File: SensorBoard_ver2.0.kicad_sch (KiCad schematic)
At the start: 64 parts, among them J1 CANConn, J10 Limit3-B, J11 USB_C, J12 Limit2-A, J13 Limit2-B, J14 Limit4-A, J15 Limit4-B, J16 Abso, J17 Abso, J18 STLink, J19 Abso, J2 CANConn, J20 Abso, J21 Abso, J22 Abso, J3 Enc1, J4 Enc2, J5 Enc3, J6 Enc4, J7 Limit1-A, J8 Limit1-B, J9 Limit3-A, SW1 CAN_Terminal, SW2 IDSetSW, SW3 Enc⇔Lim Change, SW4 ResetSW, SW5 RS485_Terminal, SW6 AbsoSW, U1 L7805, U2 ATA6561, U3 3.3V Regulator, U4 STM32F303K8Tx, U5 MAX3485, Y1 Crystal

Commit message: Add files via upload
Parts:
- removed J10: Limit3-B, Connector_JST:JST_XA_B02B-XASK-1_1x02_P2.50mm_Vertical, symbol Connector:Conn_01x02_Socket
- removed J12: Limit2-A, Connector_JST:JST_XA_B02B-XASK-1_1x02_P2.50mm_Vertical, symbol Connector:Conn_01x02_Socket
- removed J13: Limit2-B, Connector_JST:JST_XA_B02B-XASK-1_1x02_P2.50mm_Vertical, symbol Connector:Conn_01x02_Socket
- removed J14: Limit4-A, Connector_JST:JST_XA_B02B-XASK-1_1x02_P2.50mm_Vertical, symbol Connector:Conn_01x02_Socket
- removed J15: Limit4-B, Connector_JST:JST_XA_B02B-XASK-1_1x02_P2.50mm_Vertical, symbol Connector:Conn_01x02_Socket
- removed J7: Limit1-A, Connector_JST:JST_XA_B02B-XASK-1_1x02_P2.50mm_Vertical, symbol Connector:Conn_01x02_Socket
- removed J8: Limit1-B, Connector_JST:JST_XA_B02B-XASK-1_1x02_P2.50mm_Vertical, symbol Connector:Conn_01x02_Socket
- removed J9: Limit3-A, Connector_JST:JST_XA_B02B-XASK-1_1x02_P2.50mm_Vertical, symbol Connector:Conn_01x02_Socket
- added J?: LimitConn, Connector_JST:JST_XA_S05B-XASK-1_1x05_P2.50mm_Horizontal, symbol Connector:Conn_01x05_Socket
- J20: value Abso -> VCP
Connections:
- net IDSetSW is gone; now on net IDSet: U4.28 (PB5)
- net EncA_4: now also U4.14 (PB0)
- net EncB_4: now also U4.15 (PB1)
- net GND: now also J?.5 (Pin_5)
- net LED1: now also U4.29 (PB6); no longer U4.14 (PB0)
- net LED2: now also U4.30 (PB7); no longer U4.15 (PB1)
- net UARTTX: no longer U4.29 (PB6), U4.30 (PB7)

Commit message: 回路図の更新・PCBを作成
そんなもん
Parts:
- removed SW3: Enc⇔Lim Change, Connector_PinHeader_2.54mm:PinHeader_1x03_P2.54mm_Vertical, symbol Switch:SW_Nidec_CAS-120A1
- added J11: Limit4, Connector_JST:JST_XA_S02B-XASK-1_1x02_P2.50mm_Horizontal, symbol Connector:Conn_01x02_Socket
- added J12: Limit3, Connector_JST:JST_XA_S02B-XASK-1_1x02_P2.50mm_Horizontal, symbol Connector:Conn_01x02_Socket
- added J20: Enc5, Connector_JST:JST_XA_S04B-XASK-1_1x04_P2.50mm_Horizontal, symbol Connector:Conn_01x04_Socket
- added J8: Limit1, Connector_JST:JST_XA_S02B-XASK-1_1x02_P2.50mm_Horizontal, symbol Connector:Conn_01x02_Socket
- added J9: Limit2, Connector_JST:JST_XA_S02B-XASK-1_1x02_P2.50mm_Horizontal, symbol Connector:Conn_01x02_Socket
- added JP2: FB-Short, Jumper:SolderJumper-2_P1.3mm_Open_TrianglePad1.0x1.5mm, symbol Jumper:SolderJumper_2_Open
- J17: renamed from J20; footprint Connector_JST:JST_XA_S04B-XASK-1_1x04_P2.50mm_Horizontal -> Connector_JST:JST_XA_B04B-XASK-1_1x04_P2.50mm_Vertical
- JP1: footprint Jumper:SolderJumper-2_P1.3mm_Open_RoundedPad1.0x1.5mm -> Jumper:SolderJumper-2_P1.3mm_Open_TrianglePad1.0x1.5mm
- gave numbers to parts that had none: 1
- renumbered J11 to J10, J16 to J13, J17 to J14, J18 to J15, J19 to J16, J21 to J18, J22 to J19
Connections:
- net +3.3V: now also JP2.1 (A)
- net +3.3VA: now also JP2.2 (B)
- net +5V: now also J20.1 (Pin_1)
- net GND: now also J11.2 (Pin_2), J12.2 (Pin_2), J20.4 (Pin_4), J8.2 (Pin_2), J9.2 (Pin_2)
- net Limit1: now reaches J7.1 (Pin_1)
- net Limit1: now also J8.1 (Pin_1)
- net Limit2: now reaches J7.2 (Pin_2)
- net Limit2: now also J9.1 (Pin_1)
- net Limit3: now reaches J7.3 (Pin_3)
- net Limit3: now also J12.1 (Pin_1)
- net Limit4: now reaches J7.4 (Pin_4)
- net Limit4: now also J11.1 (Pin_1)
- net LED1 renamed EncA_5
- net EncA_5: now also J20.2 (Pin_2)
- net LED2 renamed EncB_5
- net EncB_5: now also J20.3 (Pin_3)
- net LimitMode: no longer names the net of U4.9 (PA3)
- no-connect marks 5 -> 4
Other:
- note removed: "Enc⇔Limit Change"
- moved on the sheet: J17, J7

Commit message: 基板作成
締まらない、なんか違う
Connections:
- net +3.3V: now also U3.4 (OUT)
- net AbsoSW: now also U4.6 (PA0); no longer U4.27 (PB4)
- net EncA_1: now also U4.27 (PB4); no longer U4.6 (PA0)
- net EncB_1: now also U4.28 (PB5); no longer U4.7 (PA1)
- net IDSet: now also U4.7 (PA1); no longer U4.28 (PB5)
- net LED: now reaches U4.9 (PA3)
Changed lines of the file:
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@@
 	)
 	(junction
+		(at 91.44 82.55)
+		(diameter 0)
+		(color 0 0 0 0)
+	)
+	(junction
 		(at 222.25 151.13)
 		(diameter 0)
@@
 	)
 	(junction
-		(at 91.44 83.82)
+		(at 109.22 81.28)
 		(diameter 0)
 		(color 0 0 0 0)
@@
 	(wire
 		(pts
-			(xy 125.73 66.04) (xy 133.35 66.04)
-		)
-		(stroke
-			(width 0)
-			(type default)
-		)
-	)
-	(wire
-		(pts
 			(xy 223.52 125.73) (xy 224.79 125.73)
 		)
@@
 	(wire
 		(pts
+			(xy 91.44 82.55) (xy 91.44 83.82)
+		)
+		(stroke
+			(width 0)
+			(type default)
+		)
+	)
+	(wire
+		(pts
 			(xy 26.67 50.8) (xy 25.4 50.8)
 		)
@@
 	(wire
 		(pts
-			(xy 91.44 82.55) (xy 91.44 83.82)
+			(xy 91.44 81.28) (xy 91.44 82.55)
 		)
 		(stroke
@@
 	(wire
 		(pts
-			(xy 163.83 48.26) (xy 172.72 48.26)
-		)
-		(stroke
-			(width 0)
-			(type default)
-		)
-	)
-	(wire
-		(pts
 			(xy 125.73 60.96) (xy 133.35 60.96)
 		)
@@
 	(wire
 		(pts
+			(xy 109.22 81.28) (xy 109.22 83.82)
+		)
+		(stroke
+			(width 0)
+			(type default)
+		)
+	)
+	(wire
+		(pts
 			(xy 58.42 87.63) (xy 58.42 88.9)
 		)
@@
 	(wire
 		(pts
+			(xy 125.73 66.04) (xy 133.35 66.04)
+		)
+		(stroke
+			(width 0)
+			(type default)
+		)
+	)
+	(wire
+		(pts
 			(xy 46.99 173.99) (xy 45.72 173.99)
 		)
@@
 	(wire
 		(pts
+			(xy 107.95 81.28) (xy 109.22 81.28)
+		)
+		(stroke
+			(width 0)
+			(type default)
+		)
+	)
+	(wire
+		(pts
+			(xy 163.83 40.64) (xy 172.72 40.64)
+		)
+		(stroke
+			(width 0)
+			(type default)
+		)
+	)
+	(wire
+		(pts
 			(xy 207.01 64.77) (xy 207.01 66.04)
 		)
@@
 	(wire
 		(pts
-			(xy 163.83 43.18) (xy 172.72 43.18)
+			(xy 205.74 88.9) (xy 205.74 91.44)
 		)
 		(stroke
@@
 	(wire
 		(pts
-			(xy 205.74 88.9) (xy 205.74 91.44)
+			(xy 243.84 125.73) (xy 245.11 125.73)
 		)
 		(stroke
@@
 	(wire
 		(pts
-			(xy 243.84 125.73) (xy 245.11 125.73)
+			(xy 163.83 48.26) (xy 172.72 48.26)
 		)
 		(stroke
@@
 	(wire
 		(pts
-			(xy 91.44 83.82) (xy 92.71 83.82)
-		)
-		(stroke
-			(width 0)
-			(type default)
-		)
-	)
-	(wire
-		(pts
 			(xy 215.9 55.88) (xy 217.17 55.88)
 		)
@@
 	(wire
 		(pts
-			(xy 40.64 83.82) (xy 39.37 83.82)
+			(xy 91.44 82.55) (xy 92.71 82.55)
 		)
 		(stroke
@@
 	(wire
 		(pts
-			(xy 261.62 151.13) (xy 267.97 151.13)
+			(xy 40.64 83.82) (xy 39.37 83.82)
 		)
 		(stroke
@@
 	(wire
 		(pts
-			(xy 39.37 168.91) (xy 46.99 168.91)
+			(xy 261.62 151.13) (xy 267.97 151.13)
 		)
 		(stroke
@@
 	(wire
 		(pts
-			(xy 267.97 156.21) (xy 267.97 153.67)
+			(xy 39.37 168.91) (xy 46.99 168.91)
 		)
 		(stroke
@@
 	(wire
 		(pts
-			(xy 205.74 156.21) (xy 204.47 156.21)
+			(xy 267.97 156.21) (xy 267.97 153.67)
 		)
 		(stroke
@@
 	(wire
 		(pts
-			(xy 109.22 82.55) (xy 109.22 83.82)
+			(xy 205.74 156.21) (xy 204.47 156.21)
 		)
 		(stroke
@@
 	(wire
 		(pts
+			(xy 163.83 43.18) (xy 172.72 43.18)
+		)
+		(stroke
+			(width 0)
+			(type default)
+		)
+	)
+	(wire
+		(pts
 			(xy 240.03 153.67) (xy 240.03 156.21)
 		)
@@
 	(wire
 		(pts
+			(xy 125.73 68.58) (xy 133.35 68.58)
+		)
+		(stroke
+			(width 0)
+			(type default)
+		)
+	)
+	(wire
+		(pts
 			(xy 125.73 40.64) (xy 133.35 40.64)
 		)
@@
 	(wire
 		(pts
-			(xy 163.83 40.64) (xy 172.72 40.64)
-		)
-		(stroke
-			(width 0)
-			(type default)
-		)
-	)
-	(wire
-		(pts
 			(xy 67.31 173.99) (xy 66.04 173.99)
 		)
@@
 	(wire
 		(pts
-			(xy 125.73 68.58) (xy 133.35 68.58)
-		)
-		(stroke
-			(width 0)
-			(type default)
-		)
-	)
-	(wire
-		(pts
 			(xy 59.69 168.91) (xy 67.31 168.91)
 		)
@@
 		)
 	)
+	(label "IDSet"
+		(at 172.72 43.18 180)
+		(effects
+			(font
+				(size 1.27 1.27)
+			)
+			(justify right bottom)
+		)
+	)
 	(label "EncB_4"
 		(at 125.73 60.96 0)
@@
 		)
 	)
-	(label "EncA_1"
-		(at 172.72 40.64 180)
-		(effects
-			(font
-				(size 1.27 1.27)
-			)
-			(justify right bottom)
-		)
-	)
 	(label "CANL"
 		(at 33.02 55.88 180)
@@
 		)
 	)
+	(label "AbsoSW"
+		(at 172.72 40.64 180)
+		(effects
+			(font
+				(size 1.27 1.27)
+			)
+			(justify right bottom)
+		)
+	)
 	(label "CANL"
 		(at 33.02 34.29 180)
@@
 		)
 	)
+	(label "EncB_1"
+		(at 125.73 68.58 0)
+		(effects
+			(font
+				(size 1.27 1.27)
+			)
+			(justify left bottom)
+		)
+	)
 	(label "EncB_2"
 		(at 172.72 53.34 180)
@@
 		)
 	)
-	(label "CANTX"
-		(at 172.72 71.12 180)
+	(label "LED"
+		(at 172.72 48.26 180)
 		(effects
 			(font
@@
 		)
 	)
-	(label "EncB_5"
-		(at 125.73 73.66 0)
+	(label "CANTX"
+		(at 172.72 71.12 180)
 		(effects
 			(font
 				(size 1.27 1.27)
 			)
-			(justify left bottom)
+			(justify right bottom)
 		)
 	)
-	(label "AbsoSW"
-		(at 125.73 66.04 0)
+	(label "EncB_5"
+		(at 125.73 73.66 0)
 		(effects
 			(font
@@
 		)
 	)
-	(label "IDSet"
-		(at 125.73 68.58 0)
+	(label "EncA_1"
+		(at 125.73 66.04 0)
 		(effects
 			(font
@@
 		)
 	)
-	(label "EncB_1"
-		(at 172.72 43.18 180)
-		(effects
-			(font
-				(size 1.27 1.27)
-			)
-			(justify right bottom)
-		)
-	)
 	(label "RS485_A"
 		(at 237.49 128.27 0)
@@
 	(symbol
 		(lib_id "power:VCC")
-		(at 91.44 82.55 0)
+		(at 91.44 81.28 0)
 		(unit 1)
 		(exclude_from_sim no)
@@
 		(dnp no)
 		(property "Reference" "#PWR033"
-			(at 91.44 86.36 0)
+			(at 91.44 85.09 0)
 			(effects
 				(font
@@
 		)
 		(property "Value" "VCC"
-			(at 91.44 78.74 0)
+			(at 91.44 77.47 0)
 			(effects
 				(font
@@
 		)
 		(property "Footprint" ""
-			(at 91.44 82.55 0)
+			(at 91.44 81.28 0)
 			(effects
 				(font
@@
 		)
 		(property "Datasheet" ""
-			(at 91.44 82.55 0)
+			(at 91.44 81.28 0)
 			(effects
 				(font
@@
 		)
 		(property "Description" "Power symbol creates a global label with name \"VCC\""
-			(at 91.44 82.55 0)
+			(at 91.44 81.28 0)
 			(effects
 				(font
@@
 	(symbol
 		(lib_id "power:+5V")
-		(at 109.22 82.55 0)
+		(at 109.22 81.28 0)
 		(unit 1)
 		(exclude_from_sim no)
@@
 		(dnp no)
 		(property "Reference" "#PWR039"
-			(at 109.22 86.36 0)
+			(at 109.22 85.09 0)
 			(effects
 				(font
@@
 		)
 		(property "Value" "+3.3V"
-			(at 109.22 78.74 0)
+			(at 109.22 77.47 0)
 			(effects
 				(font
@@
 		)
 		(property "Footprint" ""
-			(at 109.22 82.55 0)
+			(at 109.22 81.28 0)
 			(effects
 				(font
@@
 		)
 		(property "Datasheet" ""
-			(at 109.22 82.55 0)
+			(at 109.22 81.28 0)
 			(effects
 				(font
@@
 		)
 		(property "Description" "Power symbol creates a global label with name \"+5V\""
-			(at 109.22 82.55 0)
+			(at 109.22 81.28 0)
 			(effects
 				(font
@@
 		)
 		(property "Value" "3.3V Regulator"
-			(at 100.33 80.01 0)
+			(at 100.33 78.994 0)
 			(effects
 				(font
@@
 		(pin "1"
 		)
+		(pin "4"
+		)
 		(instances

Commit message: だいたい完成
だいたい完成しました
あとはタイプシーやらシルクやらを決めるだけ
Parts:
- removed J11: Limit4, Connector_JST:JST_XA_S02B-XASK-1_1x02_P2.50mm_Horizontal, symbol Connector:Conn_01x02_Socket
- removed J12: Limit3, Connector_JST:JST_XA_S02B-XASK-1_1x02_P2.50mm_Horizontal, symbol Connector:Conn_01x02_Socket
- removed J7: LimitConn, Connector_JST:JST_XA_S05B-XASK-1_1x05_P2.50mm_Horizontal, symbol Connector:Conn_01x05_Socket
- removed J8: Limit1, Connector_JST:JST_XA_S02B-XASK-1_1x02_P2.50mm_Horizontal, symbol Connector:Conn_01x02_Socket
- removed J9: Limit2, Connector_JST:JST_XA_S02B-XASK-1_1x02_P2.50mm_Horizontal, symbol Connector:Conn_01x02_Socket
- removed SW5: RS485_Terminal, Connector_PinHeader_2.54mm:PinHeader_1x03_P2.54mm_Vertical, symbol Switch:SW_Nidec_CAS-120A1
- R5: footprint (none) -> Resistor_SMD:R_0603_1608Metric
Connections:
- net +5V: now also C5.1, U3.3 (IN)
- net RS485_A: now also R8.2; no longer R8.1
- net RS485_B: now also R8.1
- net VCC: no longer C5.1, U3.3 (IN)
- no-connect marks 4 -> 3
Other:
- note removed: "Limit_Pin"
- moved on the sheet: C13, J13, J16, J18, J19, R6, R8, SW6, U5

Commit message: 多分最終稿
色々修正等
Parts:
- removed C13: 0.1μF, Capacitor_SMD:C_0603_1608Metric, symbol Device:C
- removed J17: VCP, Connector_JST:JST_XA_B04B-XASK-1_1x04_P2.50mm_Vertical, symbol Connector:Conn_01x04_Socket
- removed JP2: FB-Short, Jumper:SolderJumper-2_P1.3mm_Open_TrianglePad1.0x1.5mm, symbol Jumper:SolderJumper_2_Open
- removed SW4: ResetSW, symbol Switch:SW_MEC_5E
- removed SW6: AbsoSW, symbol Switch:SW_MEC_5E
- added C14: 0.1μF, Capacitor_SMD:C_0603_1608Metric, symbol Device:C
- added D4: LED, LED_SMD:LED_0603_1608Metric, symbol Device:LED
- added H5: Hamada, MySilcscreen:Hamada, symbol Mechanical:MountingHole
- added R9: 10kΩ, Resistor_SMD:R_0603_1608Metric, symbol Device:R
- added SW3: Reset, MySW:SMD_MySW1, symbol Switch:SW_MEC_5G
- added SW4: IDSetSW, Connector_PinHeader_2.54mm:PinHeader_1x03_P2.54mm_Vertical, symbol Switch:SW_Nidec_CAS-120A1
- added SW5: Terminal, Connector_PinHeader_2.54mm:PinHeader_1x03_P2.54mm_Vertical, symbol Switch:SW_Nidec_CAS-120A1
- C1, C2: value ? -> 10μF; footprint Capacitor_SMD:C_0603_1608Metric -> Capacitor_SMD:C_0805_2012Metric
- C11, C12: value C -> 33pF?
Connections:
- net EncA_5 is gone; now on net EncA_1: J20.2 (Pin_2), U4.29 (PB6)
- net EncB_5 is gone; now on net EncB_1: J20.3 (Pin_3), U4.30 (PB7)
- net +3.3V: now also C14.1
- net EncA_1: no longer J3.2 (Pin_2), U4.27 (PB4)
- net EncB_1: no longer J3.3 (Pin_3), U4.28 (PB5)
- net GND: now also C14.2, D4.1 (K), SW3.2 (B), SW3.4 (B), SW4.2 (B)
- net LED: now also R9.1
- net NRST: now also SW3.1 (A), SW3.2 (B)
- net RS485_A: now also SW5.1 (C); no longer R6.1
- net AbsoSW renamed EncSW
- net EncSW: now also SW4.1 (C)
- new net: R6.1, SW5.2 (B)
- new net: D4.2 (A), R9.2
- new net EncA_0: J3.2 (Pin_2), U4.27 (PB4)
- new net EncB_0: J3.3 (Pin_3), U4.28 (PB5)
- no-connect marks 3 -> 4
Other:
- note added: "Encorder_SW"
- note removed: "AbsoSW"
- moved on the sheet: J13, J14, J16, J18, J19, R6, R8, U5

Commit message: 大改造する前のバックアップ
大改造して、失敗したときのバックアップです
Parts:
- removed U3: 3.3V Regulator, Package_TO_SOT_SMD:SOT-223, symbol Regulator_Linear:L7805
- added IC1: MIC5504-3.3YM5-T5, SOT95P280X130-5N, symbol MIC5504-3_3YM5-T5:MIC5504-3.3YM5-T5
- added R10: 10kΩ, Resistor_SMD:R_0603_1608Metric, symbol Device:R
- C5, C6: value ? -> 1μF
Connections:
- net +3.3V: now also IC1.5 (VOUT)
- net +5V: now also IC1.1 (VIN), R10.1
- net GND: now also IC1.2 (GND)
- new net: IC1.3 (EN), R10.2
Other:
- note added: "SelectJP"
- note added: "TypeC"
- note removed: "5V Select SW"
- note removed: "PowerOnly Type-C"
- moved on the sheet: J10, JP1

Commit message: 大改造したあと　ver01
特になし、アップロードしたファイル間違えてるかもしれないくらい？
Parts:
- removed FB1: FerriteBead, Inductor_SMD:L_0603_1608Metric, symbol Device:FerriteBead
- removed SW5: Terminal, Connector_PinHeader_2.54mm:PinHeader_1x03_P2.54mm_Vertical, symbol Switch:SW_Nidec_CAS-120A1
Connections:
- net +3.3VA is gone; now on net +3.3V: U4.5 (VDDA)
- net RS485_A: now also R6.2
- net RS485_B: now also R6.1; no longer R6.2

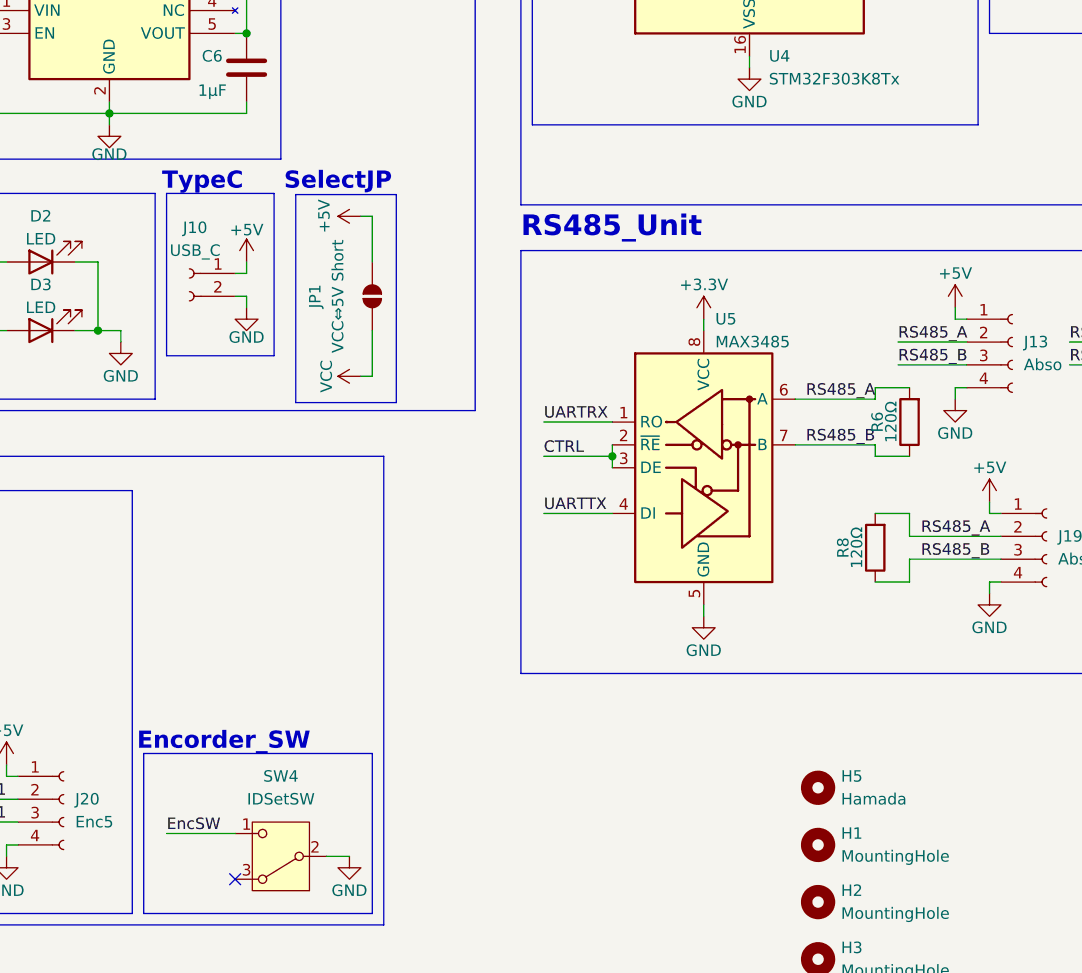
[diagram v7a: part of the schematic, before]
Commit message: ver1、完成形
なんか、いろいろ制御との兼ね合いでダメなところが出てきた…
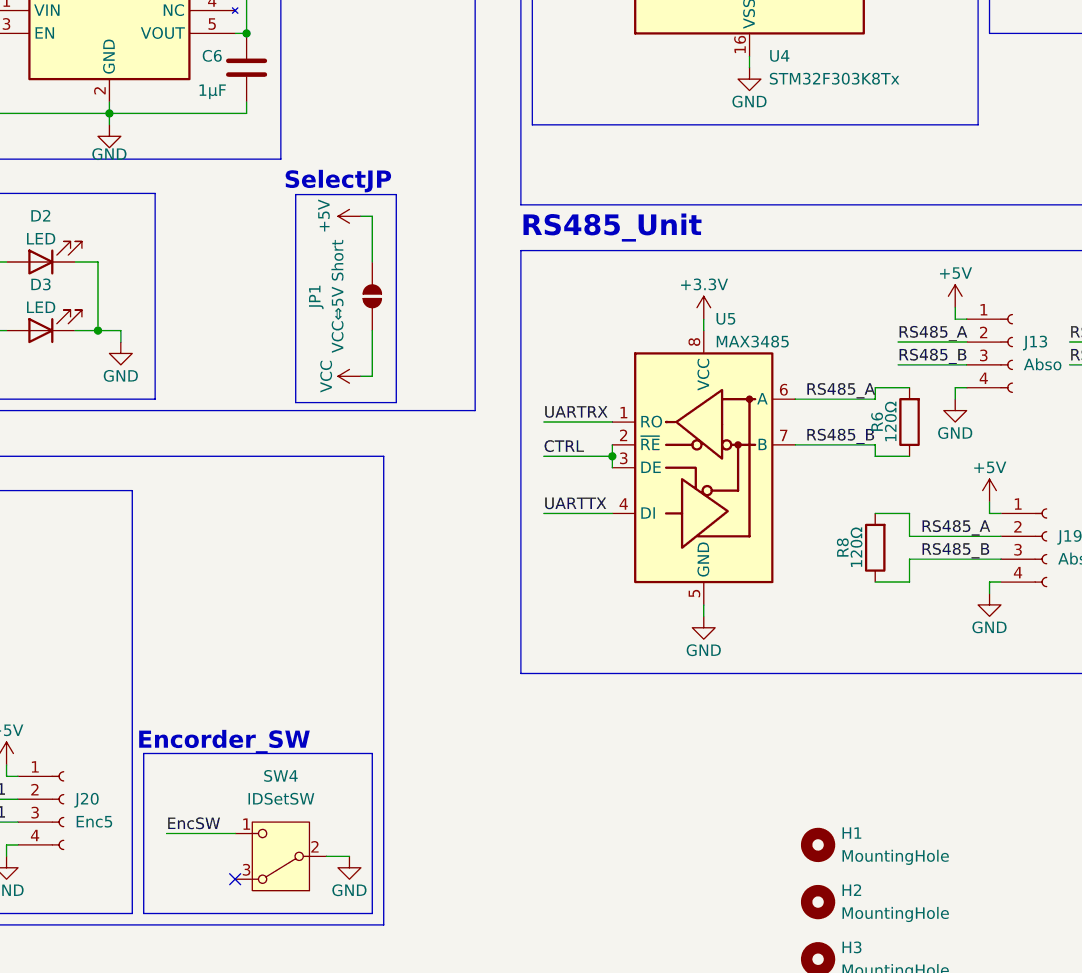
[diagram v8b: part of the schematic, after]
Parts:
- removed H5: Hamada, MySilcscreen:Hamada, symbol Mechanical:MountingHole
- removed J10: USB_C, MyUSB_C:PowerOnlyUSB_C, symbol Connector:Conn_01x02_Socket
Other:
- note removed: "TypeC"
